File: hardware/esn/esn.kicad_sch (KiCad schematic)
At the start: 9 parts, among them Q1 Q_PMOS_GSD, U1 MCP1700x-250xxTT

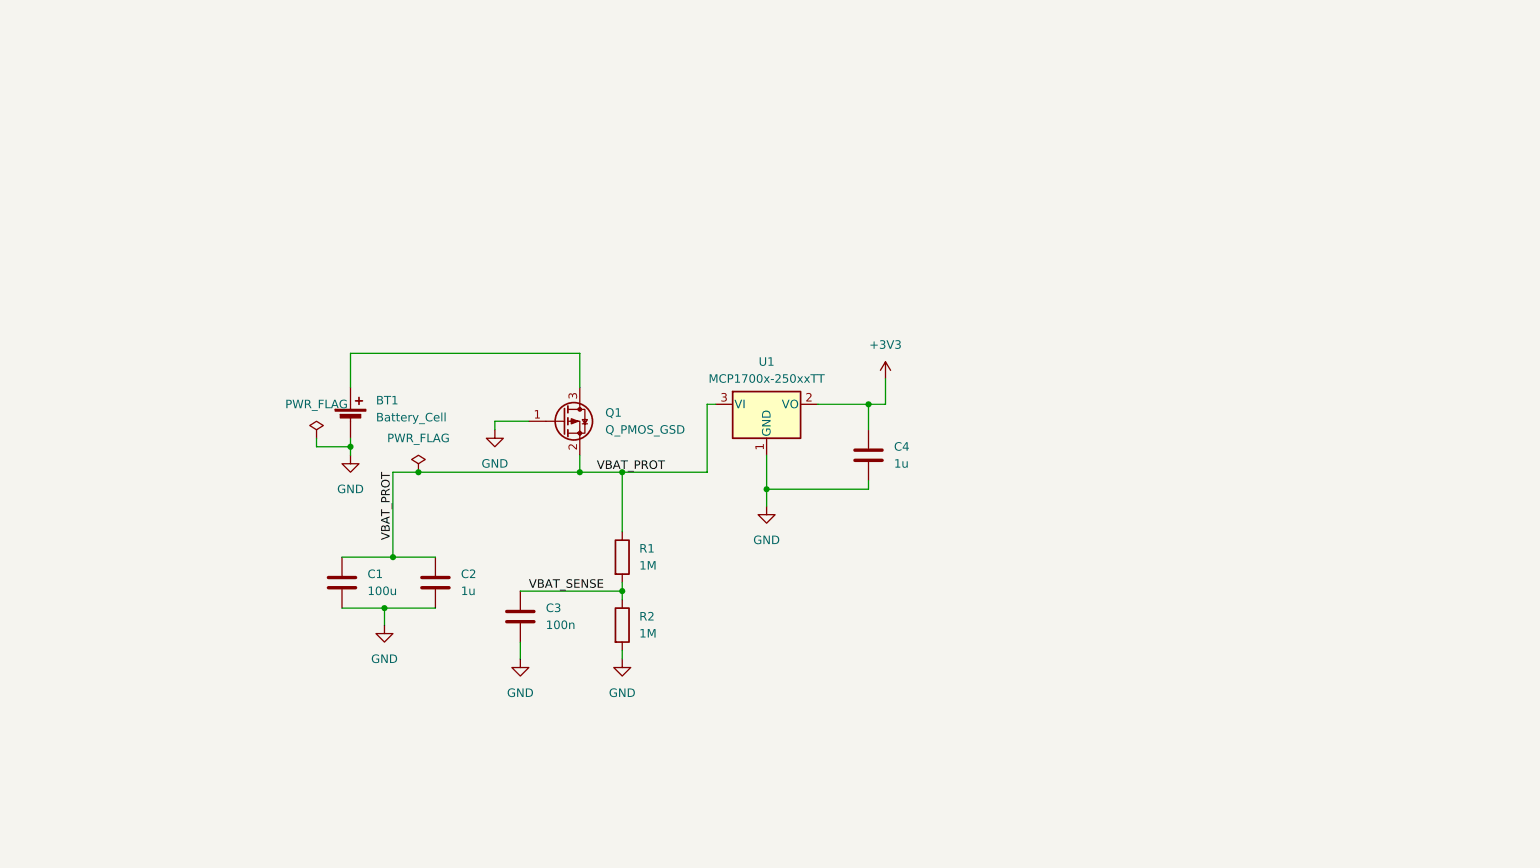
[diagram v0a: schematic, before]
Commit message: hardware: MCU decoupkinng farm complete (per-pin 100nF + bulk/VDDA/VDDRF caps)
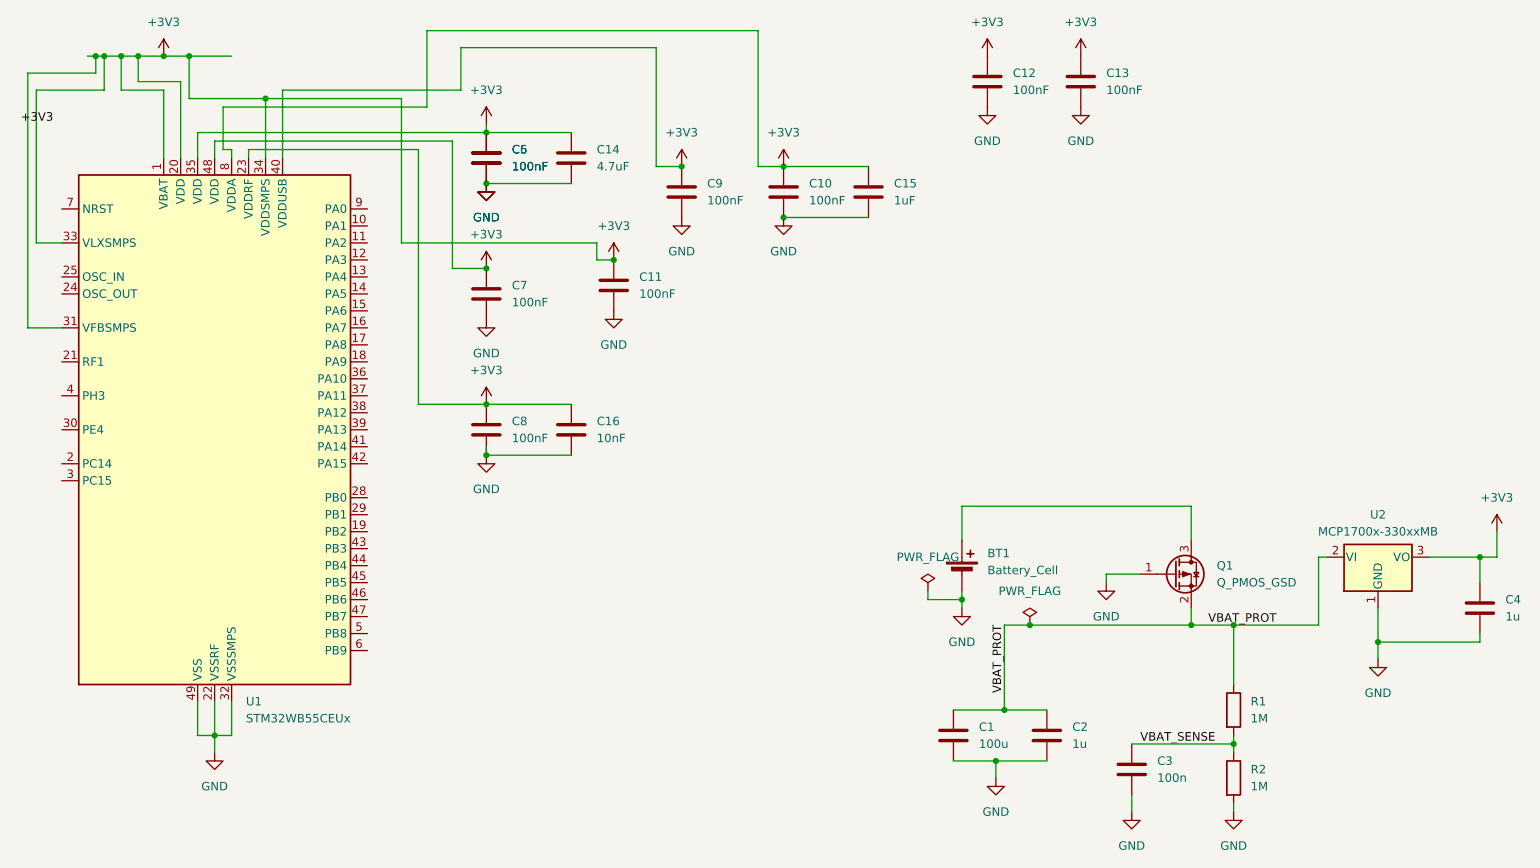
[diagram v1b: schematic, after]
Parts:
- removed U1: MCP1700x-250xxTT, Package_TO_SOT_SMD:SOT-23, symbol Regulator_Linear:MCP1700x-250xxTT
- added C10, C11, C12, C13, C5, C6, C7, C8, C9: 100nF, symbol Device:C
- added C14: 4.7uF, symbol Device:C
- added C15: 1uF, symbol Device:C
- added C16: 10nF, symbol Device:C
- added U1: STM32WB55CEUx, Package_DFN_QFN:QFN-48-1EP_7x7mm_P0.5mm_EP5.6x5.6mm, symbol MCU_ST_STM32WB:STM32WB55CEUx
- added U2: MCP1700x-330xxMB, Package_TO_SOT_SMD:SOT-89-3, symbol Regulator_Linear:MCP1700x-330xxMB
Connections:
- net +3V3: now also C10.1, C11.1, C12.1, C13.1, C14.1, C15.1, C16.1, C5.1, C6.1, C7.1, C8.1, C9.1, U1.1 (VBAT), U1.20 (VDD), U1.23 (VDDRF), U1.31 (VFBSMPS), U1.33 (VLXSMPS), U1.34 (VDDSMPS), U1.35 (VDD), U1.40 (VDDUSB), U1.48 (VDD), U1.8 (VDDA), U2.3 (VO)
- net GND: now also C10.2, C11.2, C12.2, C13.2, C14.2, C15.2, C16.2, C5.2, C6.2, C7.2, C8.2, C9.2, U1.22 (VSSRF), U1.32 (VSSSMPS), U1.49 (VSS), U2.1 (GND)
- net VBAT_PROT: now also U2.2 (VI)
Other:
- moved on the sheet: BT1, C1, C2, C3, C4, Q1, R1, R2
